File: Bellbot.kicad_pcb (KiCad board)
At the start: 4 copper layers, 150 x 144 mm, 94 parts, among them J1 Conn_01x02, J10 Conn_01x03, J11 Conn_01x03, J12 Conn_01x03, J2 Conn_01x04, J3 Conn_01x06, J4 Conn_01x06, J5 Conn_01x06, J6 Conn_01x07, J7 Jack-DC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

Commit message: stm32cubeide files added
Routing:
- net +5VD: track 35.2 -> 114.6 mm, vias 0 -> 7
- net GND: track 21.7 -> 100.1 mm, vias 61 -> 82
- net +8V: track 22.5 -> 97.1 mm
- net +3V0: track 27.7 -> 69.5 mm
- net Net-(D3-K): track 0.00 -> 16.6 mm, vias 0 -> 2
- net Net-(D2-K): track 0.00 -> 13.7 mm, vias 0 -> 2
- net Net-(D4-K): track 0.00 -> 13.0 mm, vias 0 -> 2
- net Net-(D1-K): track 0.00 -> 12.3 mm, vias 0 -> 2
- net +3.3V: track 12.7 -> 21.8 mm, vias 2 -> 3
- net Net-(D4-A): track 0.00 -> 8.27 mm
- net Net-(D3-A): track 0.00 -> 8.12 mm
- net Net-(D2-A): track 0.00 -> 7.46 mm
- net Net-(U2-EN): track 0.00 -> 6.12 mm
- net Net-(U7-FB): track 0.00 -> 4.82 mm
- net Net-(U5-FB): track 0.00 -> 4.68 mm
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
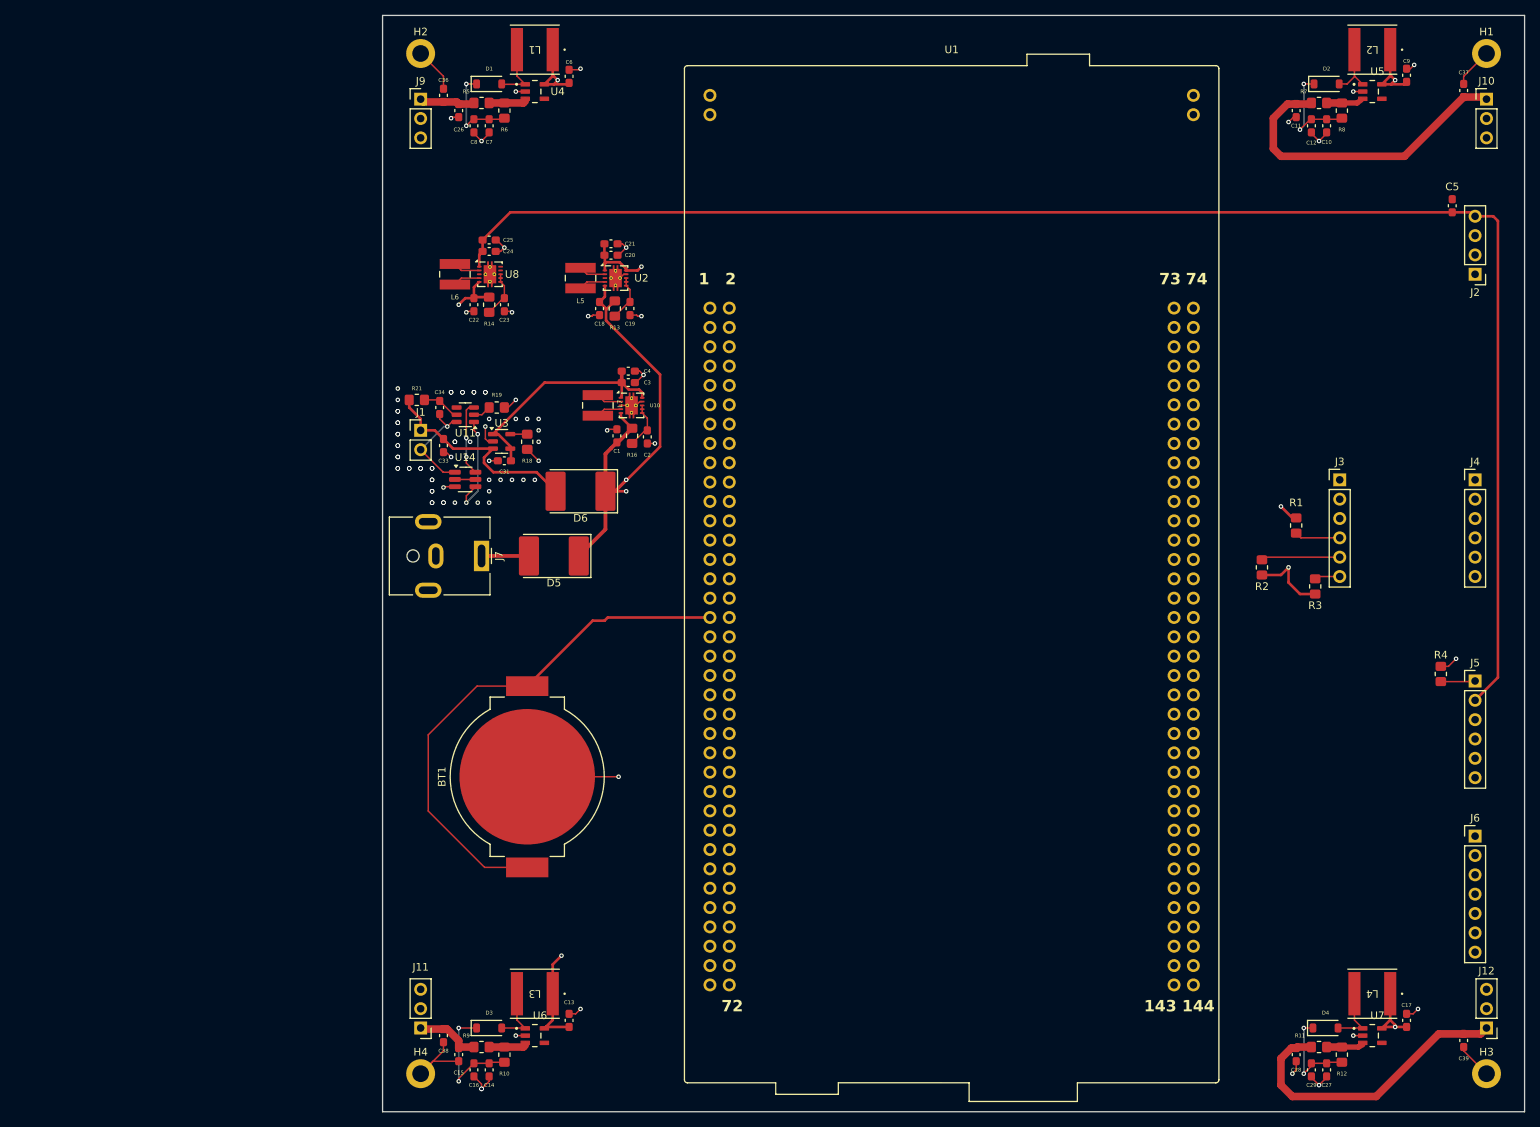
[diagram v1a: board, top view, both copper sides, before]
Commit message: General Layout Complete
Completed general layout, beginning to add debugging components such as test points and
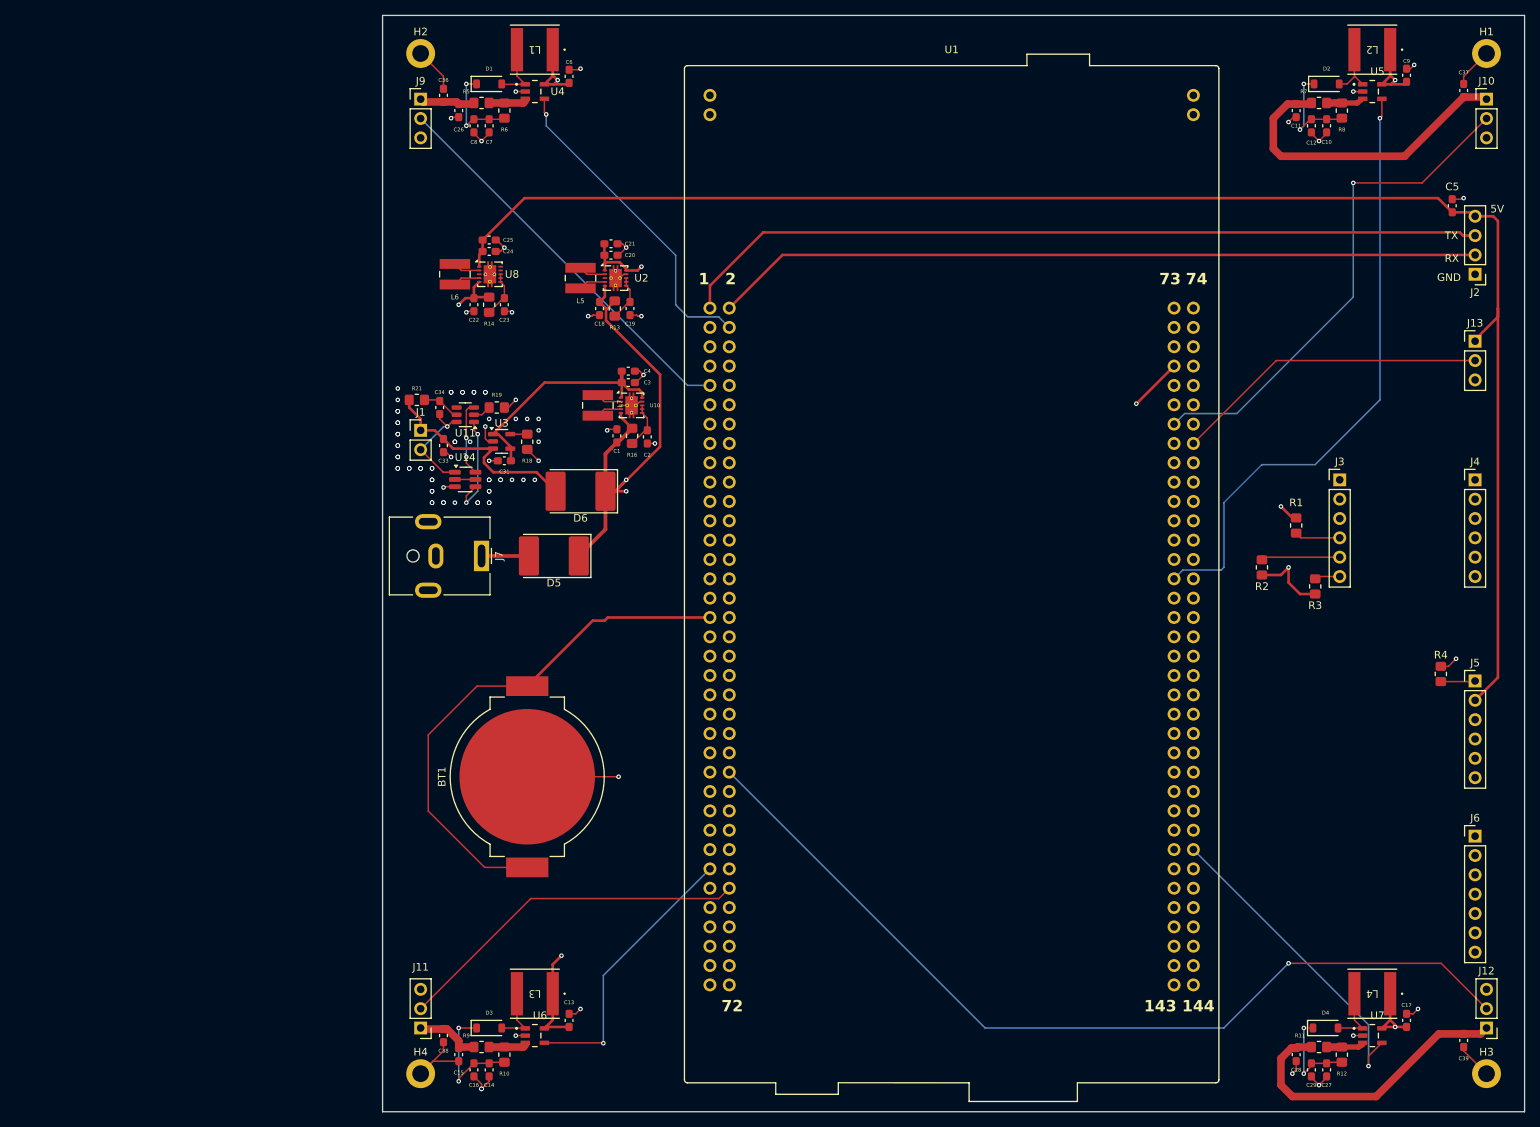
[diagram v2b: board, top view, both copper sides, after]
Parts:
- added J13: Conn_01x03, Connector_PinHeader_2.54mm:PinHeader_1x03_P2.54mm_Vertical, F.Cu at (230.0, 61.8)
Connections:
- U1 pad 11: HP_servo3 -> unconnected-(U1-PF7-Pad11)
- U1 pad 112: LP_servo1 -> unconnected-(U1-PE8-Pad112)
- U1 pad 120: 8V_REG_EN1 -> unconnected-(U1-PD15-Pad120)
- U1 pad 123: HP_servo2 -> unconnected-(U1-PE14-Pad123)
- U1 pad 124: LP_servo2 -> unconnected-(U1-PE9-Pad124)
- U1 pad 125: HP_servo1 -> unconnected-(U1-PE15-Pad125)
- U1 pad 130: 8V_REG_EN3 -> 8V_REG_EN4
- U1 pad 4: HP_servo6 -> 8V_REG_EN1
- U1 pad 40: HP_servo5 -> unconnected-(U1-PD3-Pad40)
- U1 pad 50: unconnected-(U1-PE5-Pad50) -> HP_servo4
- U1 pad 54: HP_servo4 -> unconnected-(U1-PF8-Pad54)
- U1 pad 59: 8V_REG_EN4 -> 8V_REG_EN3
- U1 pad 62: unconnected-(U1-PE6-Pad62) -> HP_servo3
- U1 pad 85: unconnected-(U1-PA6-Pad85) -> HP_servo2
- U1 pad 88: unconnected-(U1-PB12-Pad88) -> MOTOR_EN_LIDAR
- U1 pad 9: unconnected-(U1-PF6-Pad9) -> HP_servo1
- U5 pad 4: 8V_REG_EN1 -> 8V_REG_EN2
- U6 pad 4: 8V_REG_EN1 -> 8V_REG_EN3
- U7 pad 4: 8V_REG_EN1 -> 8V_REG_EN4
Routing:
- net HP_servo4: track 0.00 -> 119.4 mm, vias 0 -> 1
- net 3V3TX_LIDAR: track 0.00 -> 106.5 mm
- net 3V3RX_LIDAR: track 0.00 -> 100.9 mm
- net 8V_REG_EN2: track 0.00 -> 81.4 mm, vias 0 -> 1
- net HP_servo2: track 0.00 -> 66.5 mm, vias 0 -> 1
- net HP_servo1: track 0.00 -> 52.5 mm
- net HP_servo3: track 0.00 -> 47.1 mm
- net 8V_REG_EN1: track 0.00 -> 42.5 mm, vias 0 -> 1
- net 8V_REG_EN4: track 0.00 -> 41.7 mm, vias 0 -> 1
- net MOTOR_EN_LIDAR: track 0.00 -> 41.3 mm
- net 8V_REG_EN3: track 0.00 -> 36.5 mm, vias 0 -> 1
- net +5V: track 203.2 -> 210.4 mm
- net +3.3V: track 21.8 -> 28.8 mm, vias 3 -> 4
- net GND: track 100.1 -> 101.6 mm, vias 82 -> 93
- net (no net): vias 5 -> 0
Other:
- board text added: "5V"
- board text added: "GND"
- board text added: "RX"
- board text added: "TX"

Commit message: testpoints on board
Organized testpoints on board. Still need to fix bus for general purpose GPIO and route traces for LEDs.
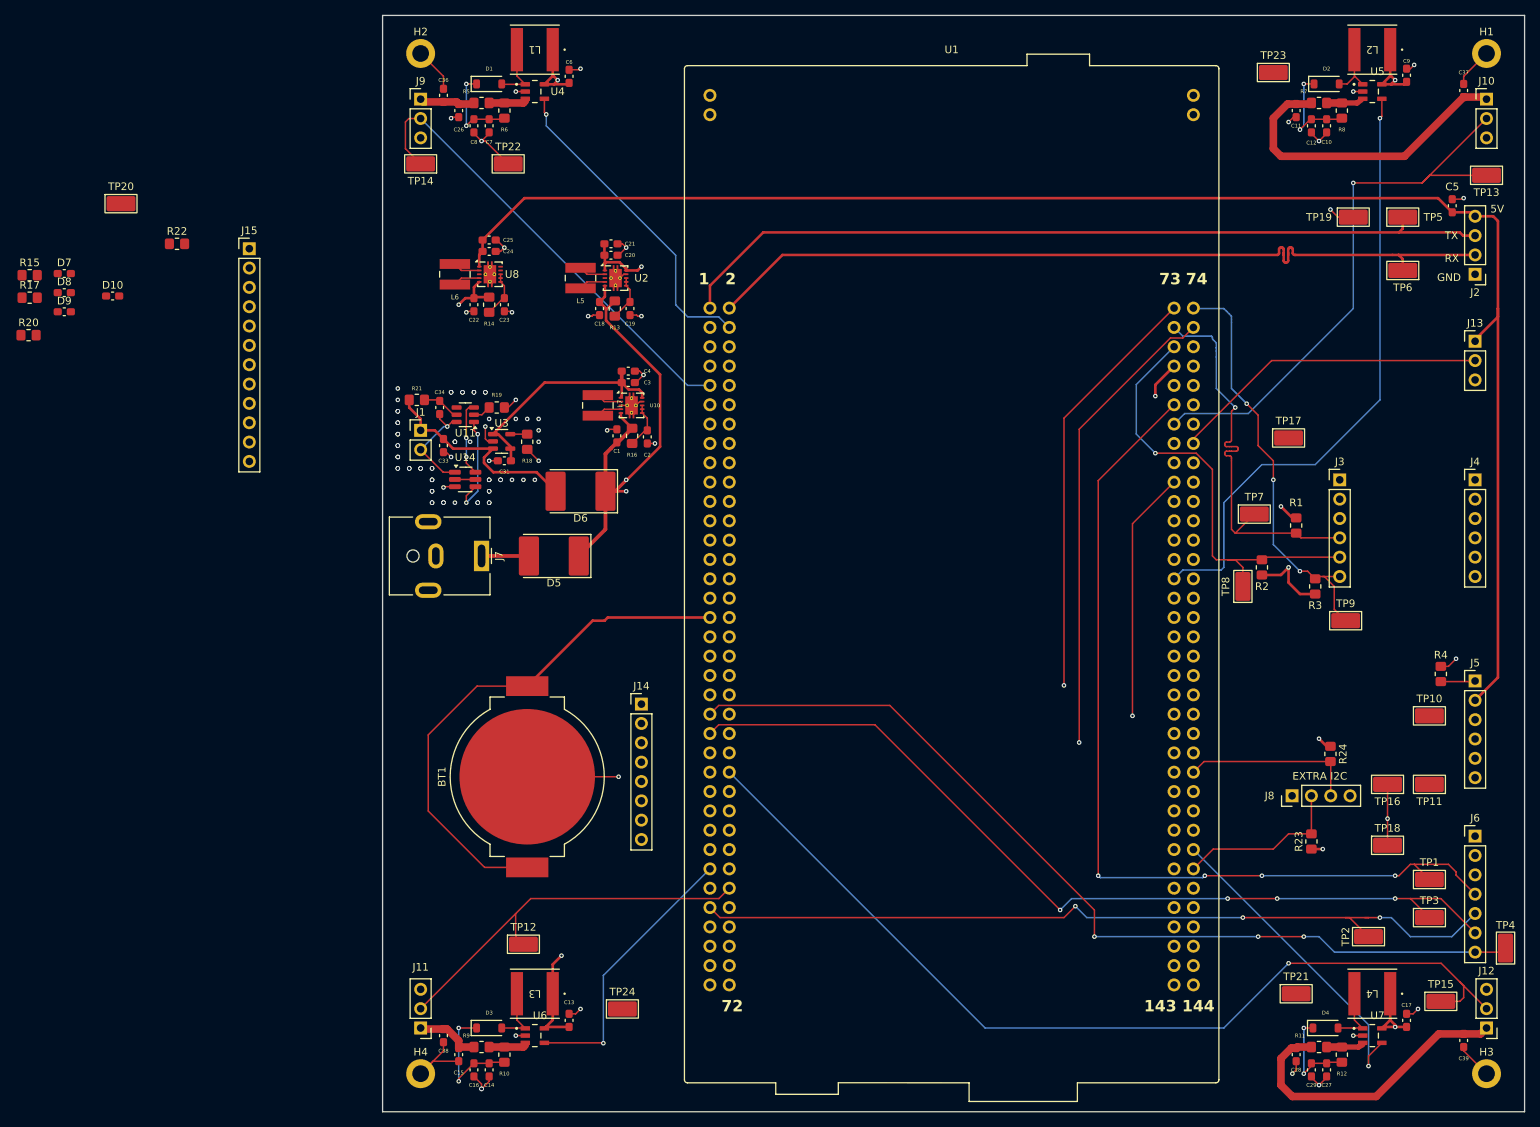
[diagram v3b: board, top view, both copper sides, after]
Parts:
- added D10: LED, Capacitor_SMD:C_0603_1608Metric_Pad1.08x0.95mm_HandSolder, F.Cu at (51.0, 55.9)
- added D7: LED, Capacitor_SMD:C_0603_1608Metric_Pad1.08x0.95mm_HandSolder, F.Cu at (44.7, 52.9)
- added D8: LED, Capacitor_SMD:C_0603_1608Metric_Pad1.08x0.95mm_HandSolder, F.Cu at (44.7, 55.4)
- added D9: LED, Capacitor_SMD:C_0603_1608Metric_Pad1.08x0.95mm_HandSolder, F.Cu at (44.7, 57.9)
- added J14: Conn_01x08, Connector_PinHeader_2.54mm:PinHeader_1x08_P2.54mm_Vertical, F.Cu at (120.5, 109.5)
- added J15: Conn_01x12, Connector_PinHeader_2.54mm:PinHeader_1x12_P2.54mm_Vertical, F.Cu at (69.0, 49.6)
- added J8: Conn_01x04, Connector_PinHeader_2.54mm:PinHeader_1x04_P2.54mm_Vertical, F.Cu at (206.0, 121.5)
- added R15: 65, Resistor_SMD:R_0805_2012Metric_Pad1.20x1.40mm_HandSolder, F.Cu at (40.1, 53.1)
- added R17: 150, Resistor_SMD:R_0805_2012Metric_Pad1.20x1.40mm_HandSolder, F.Cu at (40.1, 56.1)
- added R20: 150, Resistor_SMD:R_0805_2012Metric_Pad1.20x1.40mm_HandSolder, F.Cu at (40.0, 61.0)
- added R22: 65, Resistor_SMD:R_0805_2012Metric_Pad1.20x1.40mm_HandSolder, F.Cu at (59.5, 49.0)
- added R23: 10K, Resistor_SMD:R_0805_2012Metric_Pad1.20x1.40mm_HandSolder, F.Cu at (208.5, 127.5)
- added R24: 10K, Resistor_SMD:R_0805_2012Metric_Pad1.20x1.40mm_HandSolder, F.Cu at (211.0, 116.0)
- added TP1: SCK_SD_TP, TestPoint:TestPoint_Keystone_5019_Miniature, F.Cu at (224.0, 132.5)
- added TP10: HC05_RX_TP, TestPoint:TestPoint_Keystone_5019_Miniature, F.Cu at (224.0, 111.0)
- added TP11: HC05_TX_TP, TestPoint:TestPoint_Keystone_5019_Miniature, F.Cu at (224.0, 120.0)
- added TP12: HP3_TP, TestPoint:TestPoint_Keystone_5019_Miniature, F.Cu at (105.0, 141.0)
- added TP13: HP2_TP, TestPoint:TestPoint_Keystone_5019_Miniature, F.Cu at (231.5, 40.0)
- added TP14: HP1_TP, TestPoint:TestPoint_Keystone_5019_Miniature, F.Cu at (91.5, 38.5)
- added TP15: HP4_TP, TestPoint:TestPoint_Keystone_5019_Miniature, F.Cu at (225.5, 148.5)
- added TP16: GND_2, TestPoint:TestPoint_Keystone_5019_Miniature, F.Cu at (218.5, 120.0)
- added TP17: GND_3, TestPoint:TestPoint_Keystone_5019_Miniature, F.Cu at (205.5, 74.5)
- added TP18: GND_4, TestPoint:TestPoint_Keystone_5019_Miniature, F.Cu at (218.5, 128.0)
- added TP19: GND_5, TestPoint:TestPoint_Keystone_5019_Miniature, F.Cu at (214.0, 45.5)
- added TP2: MISO_SD_TP, TestPoint:TestPoint_Keystone_5019_Miniature, F.Cu at (216.0, 140.0)
- added TP20: GND_1, TestPoint:TestPoint_Keystone_5019_Miniature, F.Cu at (52.1, 43.7)
- added TP21: GND_6, TestPoint:TestPoint_Keystone_5019_Miniature, F.Cu at (206.5, 147.5)
- added TP22: GND_7, TestPoint:TestPoint_Keystone_5019_Miniature, F.Cu at (103.0, 38.5)
- added TP23: GND_8, TestPoint:TestPoint_Keystone_5019_Miniature, F.Cu at (203.5, 26.5)
- added TP24: GND_9, TestPoint:TestPoint_Keystone_5019_Miniature, F.Cu at (118.0, 149.5)
- added TP3: MOSI_SD_TP, TestPoint:TestPoint_Keystone_5019_Miniature, F.Cu at (224.0, 137.5)
- added TP4: CS_SD_TP, TestPoint:TestPoint_Keystone_5019_Miniature, F.Cu at (234.0, 141.5)
- added TP5: TX_LIDAR_TP, TestPoint:TestPoint_Keystone_5019_Miniature, F.Cu at (220.5, 45.5)
- added TP6: RX_LIDAR_TP, TestPoint:TestPoint_Keystone_5019_Miniature, F.Cu at (220.5, 52.5)
- added TP7: SCL_TP, TestPoint:TestPoint_Keystone_5019_Miniature, F.Cu at (201.0, 84.5)
- added TP8: SDA_TP, TestPoint:TestPoint_Keystone_5019_Miniature, F.Cu at (199.5, 94.0)
- added TP9: INT_TP, TestPoint:TestPoint_Keystone_5019_Miniature, F.Cu at (213.0, 98.5)
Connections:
- U1 pad 112: unconnected-(U1-PE8-Pad112) -> /GPIO_Gen1
- U1 pad 113: unconnected-(U1-PD13-Pad113) -> QUADSPI_IO3
- U1 pad 114: unconnected-(U1-PF10-Pad114) -> QUADSPI_CLK
- U1 pad 116: unconnected-(U1-PE7-Pad116) -> /GPIO_Gen0
- U1 pad 119: unconnected-(U1-PE10-Pad119) -> /GPIO_Gen3
- U1 pad 121: unconnected-(U1-PE12-Pad121) -> /GPIO_Gen5
- U1 pad 122: unconnected-(U1-PF14-Pad122) -> I2C_Extra_SCL
- U1 pad 123: unconnected-(U1-PE14-Pad123) -> /GPIO_Gen7
- U1 pad 124: unconnected-(U1-PE9-Pad124) -> /GPIO_Gen2
- U1 pad 125: unconnected-(U1-PE15-Pad125) -> /GPIO_Gen8
- U1 pad 127: unconnected-(U1-PE13-Pad127) -> /GPIO_Gen6
- U1 pad 128: unconnected-(U1-PE11-Pad128) -> /GPIO_Gen4
- U1 pad 132: unconnected-(U1-PF15-Pad132) -> I2C_Extra_SDA
- U1 pad 44: unconnected-(U1-PG3-Pad44) -> Net-(U1-PG3)
- U1 pad 46: unconnected-(U1-PE2-Pad46) -> QUADSPI_IO2
- U1 pad 54: unconnected-(U1-PF8-Pad54) -> QUADSPI_IO0
- U1 pad 56: unconnected-(U1-PF9-Pad56) -> QUADSPI_IO1
- U1 pad 97: unconnected-(U1-PB10-Pad97) -> QUADSPI_NCS
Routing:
- net SCK_SD: track 0.00 -> 121.0 mm, vias 0 -> 4
- net CS_SD: track 0.00 -> 120.7 mm, vias 0 -> 3
- net MOSI_SD: track 0.00 -> 117.1 mm, vias 0 -> 4
- net MISO_SD: track 0.00 -> 109.1 mm, vias 0 -> 3
- net HC05_TX: track 0.00 -> 61.7 mm, vias 0 -> 1
- net HC-05_MODE: track 4.53 -> 60.1 mm, vias 0 -> 1
- net I2C_INT: track 3.34 -> 55.6 mm, vias 0 -> 3
- net I2C_SCL: track 5.98 -> 54.9 mm, vias 0 -> 1
- net I2C_SDA: track 10.4 -> 58.8 mm, vias 0 -> 1
- net HC05_RX: track 0.00 -> 33.0 mm, vias 0 -> 1
- net I2C_Extra_SCL: track 0.00 -> 23.1 mm
- net I2C_Extra_SDA: track 0.00 -> 22.4 mm
- net GND: track 101.6 -> 117.8 mm, vias 93 -> 95
- net HP_servo2: track 66.5 -> 76.2 mm
- net HP_servo1: track 52.5 -> 61.0 mm
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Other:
- board text added: "EXTRA I2C"
